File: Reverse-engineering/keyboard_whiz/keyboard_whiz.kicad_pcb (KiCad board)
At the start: 2 copper layers, 72.8 x 56 mm, 27 parts, among them J1 I2C, J2 0.5mm, J3 0.8mm, J4 1mm, J5 Raspberry_Pi_2_3, SW1 32-39 switch, U1 0x21, U2 0x22

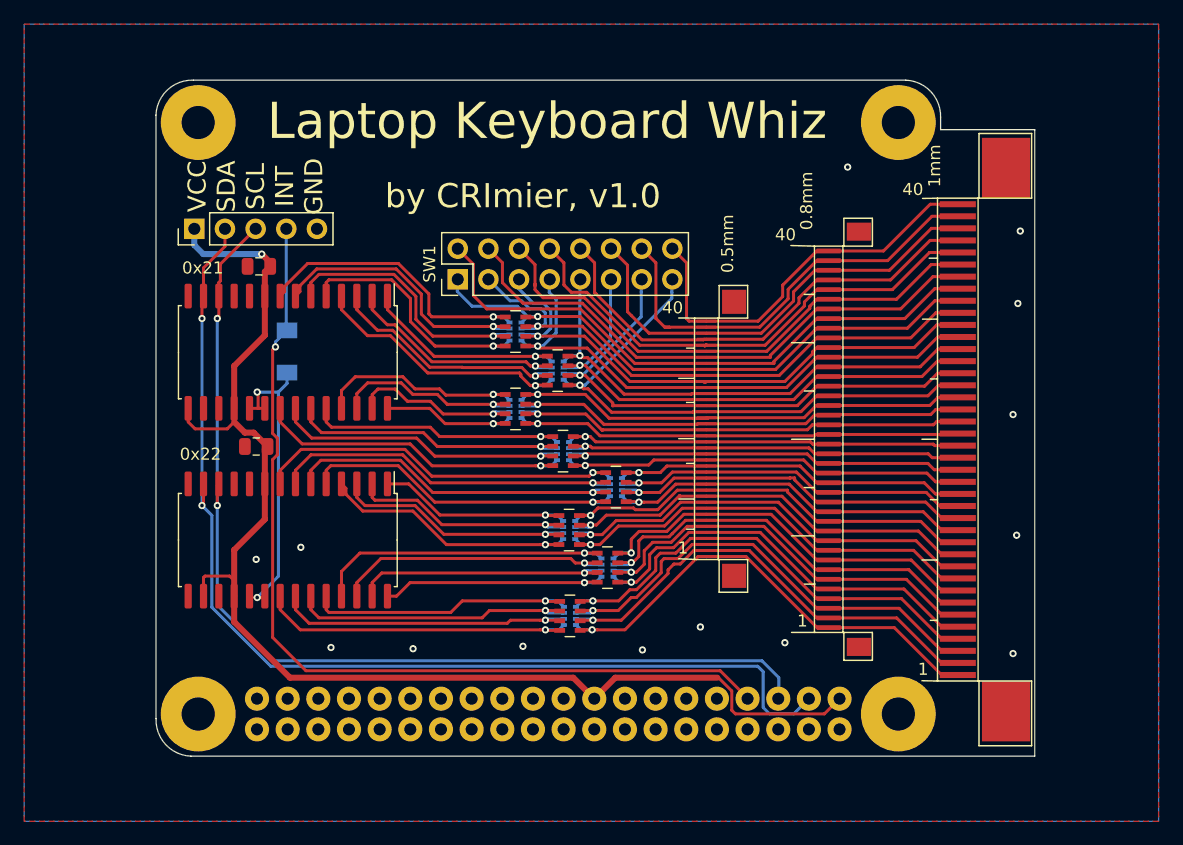
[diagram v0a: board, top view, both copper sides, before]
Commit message: Latest revision of Keyboard Whiz - one that went into v1 production
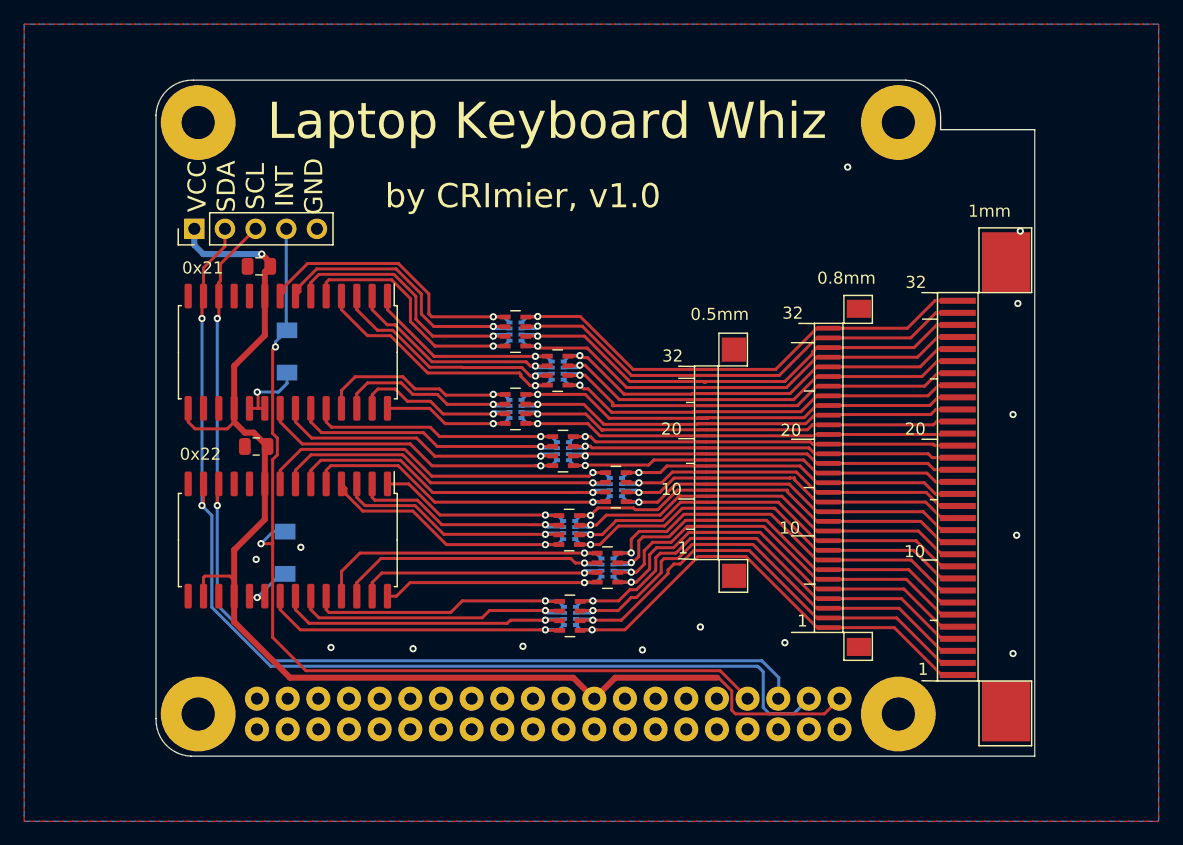
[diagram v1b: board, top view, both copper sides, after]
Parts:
- removed SW1: 32-39 switch, Connector_PinHeader_2.54mm:PinHeader_2x08_P2.54mm_Vertical
- added D2: 1N4148, Diode_SMD:D_MiniMELF, B.Cu at (141.0, 104.8)
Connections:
- D1 pad 1: INTO -> INTO1
- J5 pad 10: (no net) -> Net-(J5-Pad10)
- J5 pad 11: (no net) -> Net-(J5-Pad11)
- J5 pad 12: (no net) -> Net-(J5-Pad12)
- J5 pad 13: (no net) -> Net-(J5-Pad13)
- J5 pad 15: (no net) -> Net-(J5-Pad15)
- J5 pad 16: (no net) -> Net-(J5-Pad16)
- J5 pad 18: (no net) -> Net-(J5-Pad18)
- J5 pad 19: (no net) -> Net-(J5-Pad19)
- J5 pad 2: (no net) -> Net-(J5-Pad2)
- J5 pad 21: (no net) -> Net-(J5-Pad21)
- J5 pad 22: (no net) -> Net-(J5-Pad22)
- J5 pad 23: (no net) -> Net-(J5-Pad23)
- J5 pad 24: (no net) -> Net-(J5-Pad24)
- J5 pad 26: (no net) -> Net-(J5-Pad26)
- J5 pad 27: (no net) -> Net-(J5-Pad27)
- J5 pad 28: (no net) -> Net-(J5-Pad28)
- J5 pad 29: (no net) -> Net-(J5-Pad29)
- J5 pad 31: (no net) -> Net-(J5-Pad31)
- J5 pad 32: (no net) -> Net-(J5-Pad32)
- J5 pad 33: (no net) -> Net-(J5-Pad33)
- J5 pad 35: (no net) -> Net-(J5-Pad35)
- J5 pad 36: (no net) -> Net-(J5-Pad36)
- J5 pad 37: (no net) -> Net-(J5-Pad37)
- J5 pad 38: (no net) -> Net-(J5-Pad38)
- J5 pad 4: (no net) -> Net-(J5-Pad4)
- J5 pad 40: (no net) -> Net-(J5-Pad40)
- J5 pad 8: (no net) -> Net-(J5-Pad8)
- U1 pad 11: (no net) -> Net-(U1-Pad11)
- U1 pad 14: (no net) -> Net-(U1-Pad14)
- U1 pad 19: INTO -> INTO1
- U1 pad 20: INTO -> INTO1
- U2 pad 11: (no net) -> Net-(U2-Pad11)
- U2 pad 14: (no net) -> Net-(U2-Pad14)
- U2 pad 19: INTO -> INTO2
- U2 pad 20: INTO -> INTO2
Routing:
- net /C32: track 49.5 -> 0.00 mm
- net /C33: track 46.4 -> 0.00 mm
- net /C34: track 44.3 -> 0.00 mm
- net /C35: track 41.7 -> 0.00 mm
- net /C36: track 39.7 -> 0.00 mm
- net /C37: track 38.3 -> 0.00 mm
- net /C38: track 36.2 -> 0.00 mm
- net /C39: track 33.4 -> 0.00 mm
- net INTO: track 25.4 -> 0.00 mm, vias 2 -> 0
- net /C24: track 47.9 -> 35.7 mm
- net /C25: track 46.3 -> 36.0 mm
- net /C26: track 44.7 -> 36.2 mm
- net /C31: track 49.3 -> 41.5 mm
- net /C30: track 48.6 -> 41.1 mm
- net /C29: track 47.9 -> 40.8 mm
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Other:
- board text added: "10"
- board text added: "20"
- board text added: "32"
- board text removed: "40"

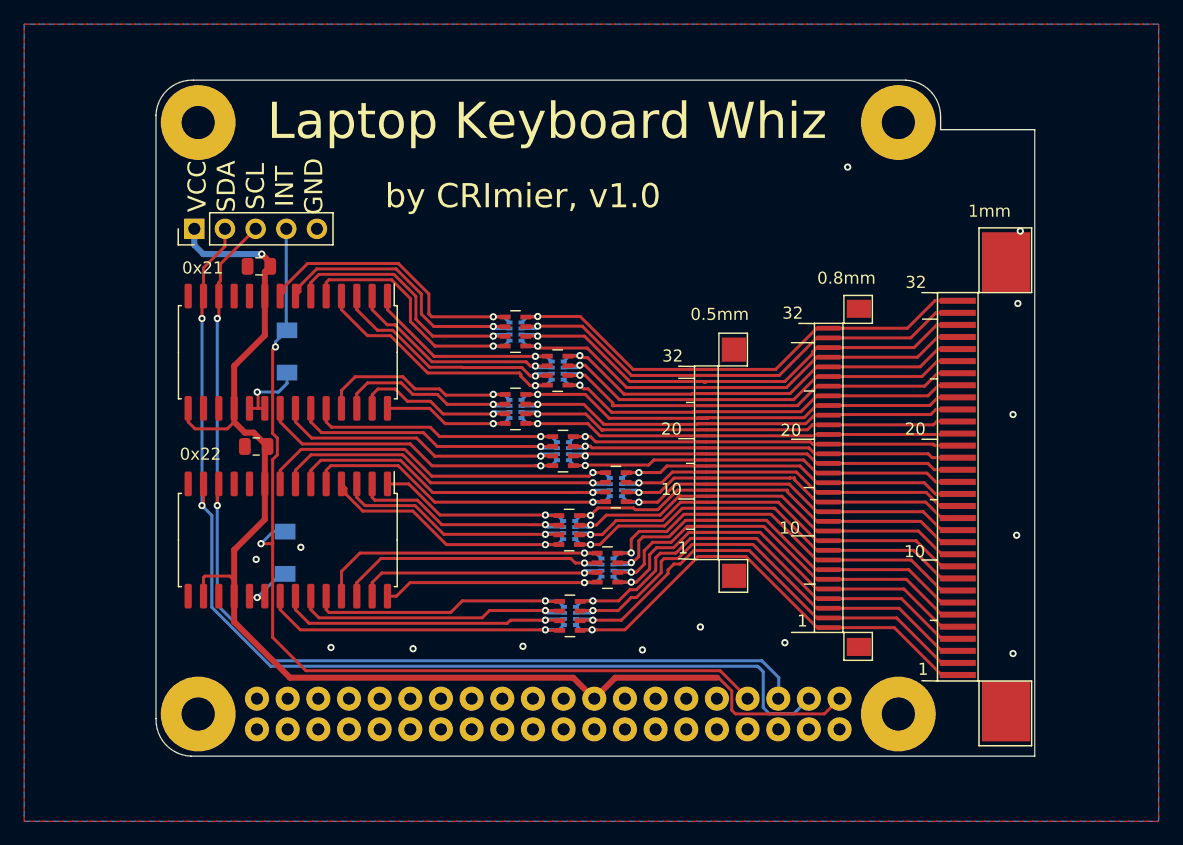
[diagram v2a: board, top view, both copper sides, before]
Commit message: Adding v2 of KeyboardWhiz (never manufactured)
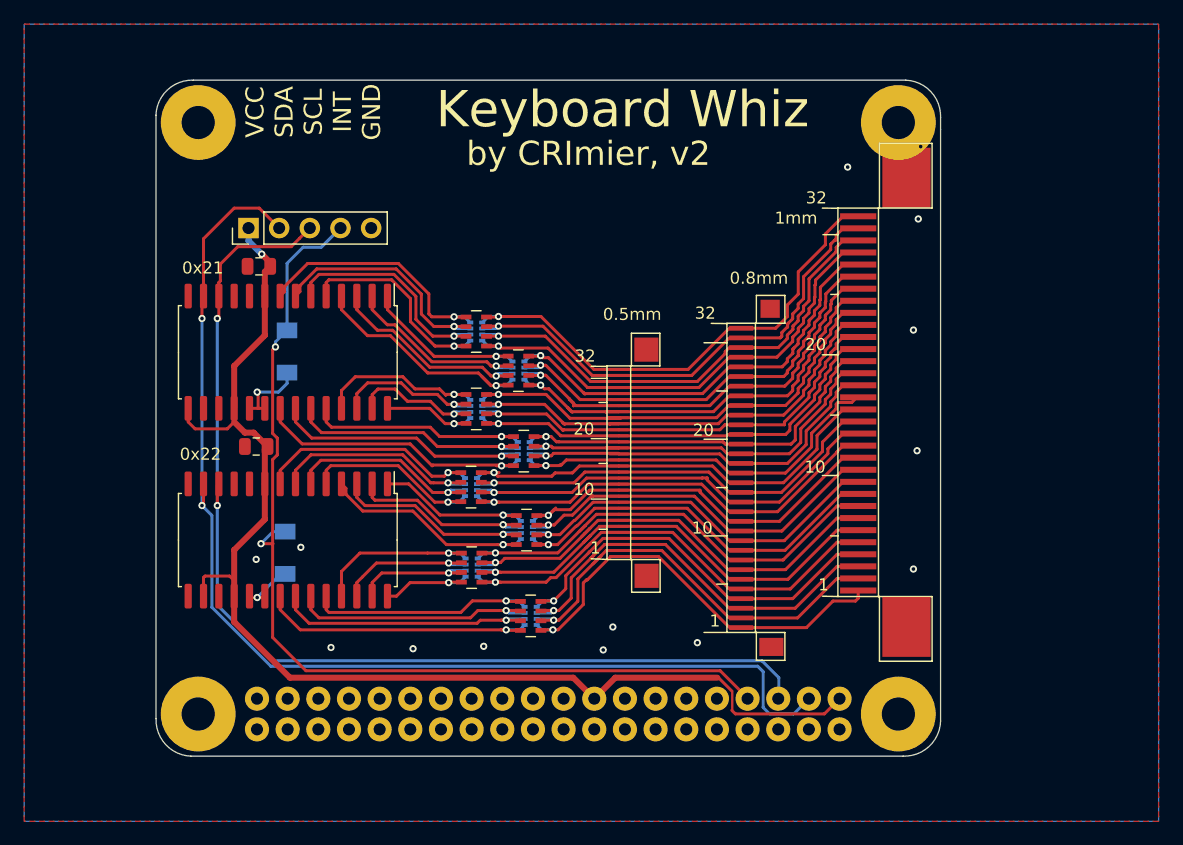
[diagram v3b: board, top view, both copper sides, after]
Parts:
- moved RN14 12.0 mm to (156.4, 99.3)
- moved RN6 12.0 mm to (156.4, 99.3)
- moved RN16 11.2 mm to (156.5, 106.0)
- moved RN8 11.2 mm to (156.5, 106.0)
- moved J4 10.8 mm to (188.5, 88.4)
- moved J2 7.25 mm to (168.6, 95.3)
- moved J3 7.25 mm to (178.8, 95.4)
- moved J1 4.49 mm to (138.0, 77.9)
- moved RN13 3.53 mm to (161.0, 102.9)
- moved RN5 3.50 mm to (161.0, 102.9)
- moved RN1 3.25 mm to (160.3, 89.7)
- moved RN10 3.25 mm to (156.8, 86.4)
- moved RN11 3.25 mm to (160.8, 96.3)
- moved RN12 3.25 mm to (156.8, 92.8)
- moved RN15 3.25 mm to (161.3, 110.0)
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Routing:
- net Net-(RN14-Pad8): track 27.3 -> 15.3 mm
- net Net-(RN14-Pad7): track 28.5 -> 16.5 mm
- net Net-(RN14-Pad6): track 29.8 -> 17.8 mm
- net Net-(RN14-Pad5): track 31.4 -> 19.4 mm
- net Net-(RN16-Pad6): track 23.5 -> 11.9 mm
- net Net-(RN16-Pad5): track 25.5 -> 14.2 mm
- net Net-(RN16-Pad8): track 19.5 -> 8.22 mm
- net Net-(RN16-Pad7): track 21.6 -> 10.4 mm
- net SDA: track 89.7 -> 96.1 mm
- net /C15: track 30.3 -> 36.5 mm
- net /C3: track 39.1 -> 33.5 mm
- net /C2: track 39.3 -> 34.0 mm
- net /C13: track 30.9 -> 36.2 mm
- net /C14: track 30.5 -> 35.7 mm
- net /C0: track 39.4 -> 34.5 mm
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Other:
- board size 72.8 x 56 mm -> 65 x 56 mm
- net class Default: clearance 0.2 -> 0.19
- rule trace_clearance: 0.2 -> 0.19
- board text added: "Keyboard Whiz"
- board text added: "by CRImier, v2"
- board text removed: "Laptop Keyboard Whiz"
- board text removed: "by CRImier, v1.0"

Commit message: keyboardwhiz: v3, a RP2040+expanders version that also allows for some chip shortage failsafes
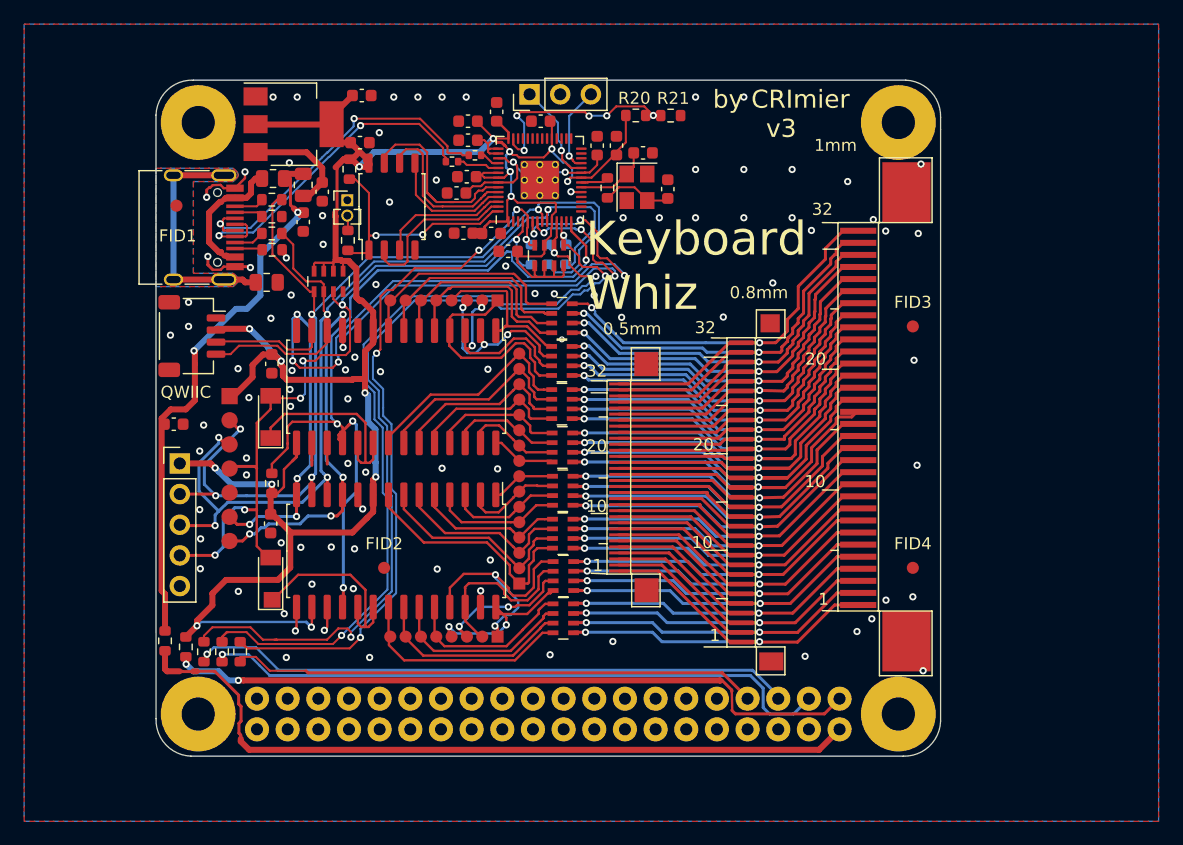
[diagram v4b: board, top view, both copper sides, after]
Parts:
- removed RN3, RN4, RN5, RN6, RN7, RN8: R_Pack04, Resistor_SMD:R_Array_Concave_4x0402
- added C10: 100nF, Capacitor_SMD:C_0603_1608Metric, F.Cu at (162.2, 69.0)
- added C11: 100nF, Capacitor_SMD:C_0603_1608Metric, F.Cu at (156.1, 73.6)
- added C12: 100nF, Capacitor_SMD:C_0603_1608Metric, F.Cu at (166.8, 71.0)
- added C13: 100nF, Capacitor_SMD:C_0603_1608Metric, F.Cu at (156.2, 69.0)
- added C14: 100nF, Capacitor_SMD:C_0603_1608Metric, F.Cu at (158.1, 78.3)
- added C15: 100nF, Capacitor_SMD:C_0603_1608Metric, F.Cu at (168.4, 71.0)
- added C16: 100nF, Capacitor_SMD:C_0603_1608Metric, F.Cu at (155.2, 75.0)
- added C17: 100nF, Capacitor_SMD:C_0603_1608Metric, F.Cu at (131.8, 94.1)
- added C18: 100nF, Capacitor_SMD:C_0603_1608Metric, F.Cu at (142.5, 77.3)
- added C19: 100nF, Capacitor_SMD:C_0603_1608Metric, F.Cu at (144.1, 74.8)
- added C20: 100nF, Capacitor_SMD:C_0603_1608Metric, F.Cu at (147.3, 66.9)
- added C3: Cc, Capacitor_SMD:C_0603_1608Metric, F.Cu at (170.7, 71.6)
- added C4: Cc, Capacitor_SMD:C_0603_1608Metric, F.Cu at (172.7, 74.6)
- added C5: 100nF, Capacitor_SMD:C_0603_1608Metric, F.Cu at (159.5, 79.8)
- added C6: 100nF, Capacitor_SMD:C_0603_1608Metric, F.Cu at (155.8, 78.3)
- added C7: 100nF, Capacitor_SMD:C_0603_1608Metric, F.Cu at (158.5, 68.2)
- added C8: 100nF, Capacitor_SMD:C_0603_1608Metric, F.Cu at (147.2, 70.8)
- added C9: 100nF, Capacitor_SMD:C_0603_1608Metric, F.Cu at (156.2, 70.6)
- added FID1: Fiducial, Fiducial:Fiducial_1mm_Mask2mm, F.Cu at (132.0, 76.0)
- added FID2: Fiducial, Fiducial:Fiducial_1mm_Mask2mm, F.Cu at (149.2, 106.0)
- added FID3: Fiducial, Fiducial:Fiducial_1mm_Mask2mm, F.Cu at (193.0, 86.0)
- added FID4: Fiducial, Fiducial:Fiducial_1mm_Mask2mm, F.Cu at (193.0, 106.0)
- added J10: SWD, Connector_PinHeader_2.54mm:PinHeader_1x03_P2.54mm_Vertical, F.Cu at (161.2, 66.8)
- added J11: BOOT, Connector_PinHeader_1.27mm:PinHeader_1x02_P1.27mm_Vertical, F.Cu at (146.2, 75.5)
- added J12: QWIIC, Connector_JST:JST_SH_SM04B-SRSS-TB_1x04-1MP_P1.00mm_Horizontal, F.Cu at (133.3, 86.8)
- added J13: IO_DT, Connector_PinHeader_2.00mm:PinHeader_1x07_P2.00mm_Vertical, F.Cu at (136.4, 91.8)
- added J6: IO_o1, Connector_PinHeader_1.27mm:PinHeader_1x08_P1.27mm_Vertical, F.Cu at (158.6, 111.7)
- added J7: IO_o2, Connector_PinHeader_1.27mm:PinHeader_1x16_P1.27mm_Vertical, F.Cu at (160.4, 107.3)
- added J8: IO_o3, Connector_PinHeader_1.27mm:PinHeader_1x08_P1.27mm_Vertical, F.Cu at (158.6, 83.8)
- added J9: USB_C_Receptacle_USB2.0, Connector_USB:USB_C_Receptacle_HRO_TYPE-C-31-M-12, F.Cu at (132.8, 77.8)
- added R1: 5K1, Resistor_SMD:R_0603_1608Metric, F.Cu at (139.9, 99.0)
- added R10: 0R, Resistor_SMD:R_0603_1608Metric, F.Cu at (139.9, 78.3)
- added R11: 0R, Resistor_SMD:R_0603_1608Metric, F.Cu at (139.9, 75.5)
- added R12: 0R, Resistor_SMD:R_0603_1608Metric, F.Cu at (132.8, 112.5)
- added R13: 0R, Resistor_SMD:R_0603_1608Metric, B.Cu at (162.8, 80.0)
- added R14: 0R, Resistor_SMD:R_0603_1608Metric, B.Cu at (164.2, 80.0)
- added R15: 0R, Resistor_SMD:R_0603_1608Metric, B.Cu at (161.4, 80.0)
- added R16: 0R, Resistor_SMD:R_0603_1608Metric, F.Cu at (135.8, 113.0)
- added R17: 0R, Resistor_SMD:R_0603_1608Metric, F.Cu at (134.3, 113.0)
- added R18: 0R, Resistor_SMD:R_0603_1608Metric, F.Cu at (137.3, 113.0)
- added R19: 0/F, Resistor_SMD:R_0805_2012Metric, F.Cu at (142.5, 74.3)
- added R2: 0/F, Resistor_SMD:R_0805_2012Metric, F.Cu at (140.0, 73.8)
- added R20: A, Resistor_SMD:R_0603_1608Metric, F.Cu at (170.1, 68.5)
- added R21: B, Resistor_SMD:R_0603_1608Metric, F.Cu at (172.9, 68.5)
- added R22: 0R, Resistor_SMD:R_0603_1608Metric, F.Cu at (131.1, 112.0)
- added R23: 0/F, Resistor_SMD:R_0805_2012Metric, F.Cu at (139.5, 82.3)
- added R3: 5K1, Resistor_SMD:R_0603_1608Metric, F.Cu at (139.9, 76.9)
- added R4: 5K1, Resistor_SMD:R_0603_1608Metric, F.Cu at (139.9, 79.7)
- added R5: 22R, Resistor_SMD:R_0402_1005Metric, F.Cu at (156.7, 71.8)
- added R6: 22R, Resistor_SMD:R_0402_1005Metric, F.Cu at (154.8, 72.3)
- added R7: 1K, Resistor_SMD:R_0603_1608Metric, F.Cu at (167.7, 74.5)
- added R8: 1K, Resistor_SMD:R_0603_1608Metric, F.Cu at (146.2, 78.9)
- added R9: 10K, Resistor_SMD:R_0603_1608Metric, F.Cu at (146.3, 73.0)
- added U3: W25Q32JVSS, Package_SO:SOIC-8_5.23x5.23mm_P1.27mm, F.Cu at (149.8, 76.1)
- added U4: RP2040, p:RP2040-QFN-56, F.Cu at (162.1, 73.9)
- added U5: AP1117-33, Package_TO_SOT_SMD:SOT-223-3_TabPin2, F.Cu at (141.7, 69.2)
- added Y1: 12MHz, Crystal:Crystal_SMD_3225-4Pin_3.2x2.5mm, F.Cu at (170.2, 74.5)
- C1, C2: footprint Capacitor_SMD:C_0805_2012Metric -> Capacitor_SMD:C_0603_1608Metric
- D1, D2: moved to F.Cu
- RN1, RN2: value R_Pack04 -> 10K; footprint Resistor_SMD:R_Array_Concave_4x0402 -> Resistor_SMD:R_Array_Concave_4x0603; moved to F.Cu
- moved J1 20.3 mm to (132.3, 97.3), turned to 0 degrees
- moved RN2 12.9 mm to (144.6, 82.3), turned to 90 degrees
- moved RN1 9.87 mm to (162.9, 80.1), turned to -90 degrees
- moved U1 9.42 mm to (150.2, 91.0)
- moved U2 9.02 mm to (150.2, 104.6)
- moved C1 8.15 mm to (139.9, 89.1), turned to -90 degrees
- moved RN16 7.63 mm to (164.1, 106.7)
- moved RN14 7.61 mm to (164.0, 99.6)
- moved RN10 7.18 mm to (163.9, 85.3)
- moved RN12 7.11 mm to (163.9, 92.4)
- moved C2 6.50 mm to (139.8, 102.3), turned to -90 degrees
- moved D1 5.59 mm to (139.8, 93.5)
- moved RN9 3.69 mm to (163.9, 88.9)
- moved RN11 3.21 mm to (164.0, 96.0)
- moved RN13 3.01 mm to (164.0, 103.2)
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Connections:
- net Net-(RN15-Pad5) renamed /O3
- net Net-(RN15-Pad6) renamed /O2
- net Net-(RN15-Pad7) renamed /O1
- net Net-(RN15-Pad8) renamed /O0
- net Net-(RN16-Pad5) renamed /O7
- net Net-(RN16-Pad6) renamed /O6
- net Net-(RN16-Pad7) renamed /O5
- net Net-(RN16-Pad8) renamed /O4
- C1 pad 1: VCC -> +3V3
- C2 pad 1: VCC -> +3V3
- J1 pad 1: VCC -> +3V3
- J5 pad 17: VCC -> Net-(J5-Pad17)
- J5 pad 2: Net-(J5-Pad2) -> +5VD
- J5 pad 3: SDA -> RSDA
- J5 pad 5: SCL -> RSCL
- J5 pad 7: INT -> RINT
- RN1 pad 1: Net-(RN1-Pad1) -> PSCL
- RN1 pad 2: Net-(RN1-Pad2) -> PSDA
- RN1 pad 3: Net-(RN1-Pad3) -> +3V3
- RN1 pad 4: Net-(RN1-Pad4) -> PINT
- RN1 pad 5: /C27 -> +3V3
- RN1 pad 6: /C26 -> +3V3
- RN1 pad 7: /C25 -> +3V3
- RN1 pad 8: /C24 -> +3V3
- RN10 pad 5: Net-(RN10-Pad5) -> /O31
- RN10 pad 6: Net-(RN10-Pad6) -> /O30
- RN10 pad 7: Net-(RN10-Pad7) -> /O29
- RN10 pad 8: Net-(RN10-Pad8) -> /O28
- RN11 pad 5: Net-(RN11-Pad5) -> /O19
- RN11 pad 6: Net-(RN11-Pad6) -> /O18
- RN11 pad 7: Net-(RN11-Pad7) -> /O17
- RN11 pad 8: Net-(RN11-Pad8) -> /O16
- RN12 pad 5: Net-(RN12-Pad5) -> /O23
- RN12 pad 6: Net-(RN12-Pad6) -> /O22
- RN12 pad 7: Net-(RN12-Pad7) -> /O21
- RN12 pad 8: Net-(RN12-Pad8) -> /O20
- RN13 pad 5: Net-(RN13-Pad5) -> /O11
- RN13 pad 6: Net-(RN13-Pad6) -> /O10
- RN13 pad 7: Net-(RN13-Pad7) -> /O9
- RN13 pad 8: Net-(RN13-Pad8) -> /O8
- RN14 pad 5: Net-(RN14-Pad5) -> /O15
- RN14 pad 6: Net-(RN14-Pad6) -> /O14
- RN14 pad 7: Net-(RN14-Pad7) -> /O13
- RN14 pad 8: Net-(RN14-Pad8) -> /O12
- RN2 pad 1: Net-(RN10-Pad8) -> SDA
- RN2 pad 2: Net-(RN10-Pad7) -> SCL
- RN2 pad 3: Net-(RN10-Pad6) -> INT
- RN2 pad 4: Net-(RN10-Pad5) -> Net-(RN2-Pad4)
- RN2 pad 5: /C31 -> +3V3
- RN2 pad 6: /C30 -> +3V3
- RN2 pad 7: /C29 -> +3V3
- RN2 pad 8: /C28 -> +3V3
- RN9 pad 5: Net-(RN1-Pad4) -> /O27
- RN9 pad 6: Net-(RN1-Pad3) -> /O26
- RN9 pad 7: Net-(RN1-Pad2) -> /O25
- RN9 pad 8: Net-(RN1-Pad1) -> /O24
- U1 pad 1: Net-(RN1-Pad4) -> /O27
- U1 pad 11: Net-(U1-Pad11) -> CS
- U1 pad 14: Net-(U1-Pad14) -> SO
- U1 pad 15: VCC -> +3V3
- U1 pad 18: VCC -> IRST
- U1 pad 2: Net-(RN1-Pad3) -> /O26
- U1 pad 21: Net-(RN11-Pad8) -> /O23
- U1 pad 22: Net-(RN11-Pad7) -> /O22
- U1 pad 23: Net-(RN11-Pad6) -> /O21
- U1 pad 24: Net-(RN11-Pad5) -> /O20
- U1 pad 25: Net-(RN12-Pad5) -> /O19
- U1 pad 26: Net-(RN12-Pad6) -> /O18
- U1 pad 27: Net-(RN12-Pad7) -> /O17
- U1 pad 28: Net-(RN12-Pad8) -> /O16
- U1 pad 3: Net-(RN1-Pad2) -> /O25
- U1 pad 4: Net-(RN1-Pad1) -> /O24
- U1 pad 5: Net-(RN10-Pad8) -> /O28
- U1 pad 6: Net-(RN10-Pad7) -> /O29
- U1 pad 7: Net-(RN10-Pad6) -> /O30
- U1 pad 8: Net-(RN10-Pad5) -> /O31
- U1 pad 9: VCC -> +3V3
- U2 pad 1: Net-(RN13-Pad5) -> /O15
- U2 pad 11: Net-(U2-Pad11) -> CS
- U2 pad 14: Net-(U2-Pad14) -> SO
- U2 pad 16: VCC -> +3V3
- U2 pad 18: VCC -> IRST
- U2 pad 2: Net-(RN13-Pad6) -> /O14
- U2 pad 3: Net-(RN13-Pad7) -> /O13
- U2 pad 4: Net-(RN13-Pad8) -> /O12
- U2 pad 5: Net-(RN14-Pad8) -> /O11
- U2 pad 6: Net-(RN14-Pad7) -> /O10
- U2 pad 7: Net-(RN14-Pad6) -> /O9
- U2 pad 8: Net-(RN14-Pad5) -> /O8
- U2 pad 9: VCC -> +3V3
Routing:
- net +3V3: track 0.00 -> 210.7 mm, vias 0 -> 15
- net SO: track 0.00 -> 74.6 mm, vias 0 -> 9
- net PSCL: track 0.00 -> 70.5 mm, vias 0 -> 3
- net PSDA: track 0.00 -> 67.5 mm, vias 0 -> 3
- net IRST: track 0.00 -> 67.2 mm, vias 0 -> 4
- net CS: track 0.00 -> 66.7 mm, vias 0 -> 8
- net +5VD: track 0.00 -> 64.5 mm
- net PINT: track 0.00 -> 60.7 mm, vias 0 -> 5
- net RSDA: track 0.00 -> 52.7 mm, vias 0 -> 1
- net RSCL: track 0.00 -> 50.4 mm, vias 0 -> 1
- net +5V: track 0.00 -> 46.6 mm, vias 0 -> 2
- net VCC: track 104.5 -> 58.0 mm, vias 1 -> 2
- net RINT: track 0.00 -> 43.5 mm
- net D-: track 0.00 -> 29.5 mm, vias 0 -> 2
- net D+: track 0.00 -> 28.7 mm, vias 0 -> 2
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- added copper zone on B.Cu, net /SHD
- added copper zone on F.Cu, net /SHD
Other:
- net class Default removed
- board text added: "QWIIC"
- board text added: "by CRImier v3"
- board text added: "by CRImier, v3"
- board text removed: "by CRImier, v2"
